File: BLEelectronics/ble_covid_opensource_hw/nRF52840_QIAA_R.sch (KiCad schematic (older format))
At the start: 37 parts, among them J3 Conn_02x05_Odd_Even, SW1 NO, SW2 SW_MEC_5G, U5 nRF52840, X1 32MHz, X2 32.768KHZ

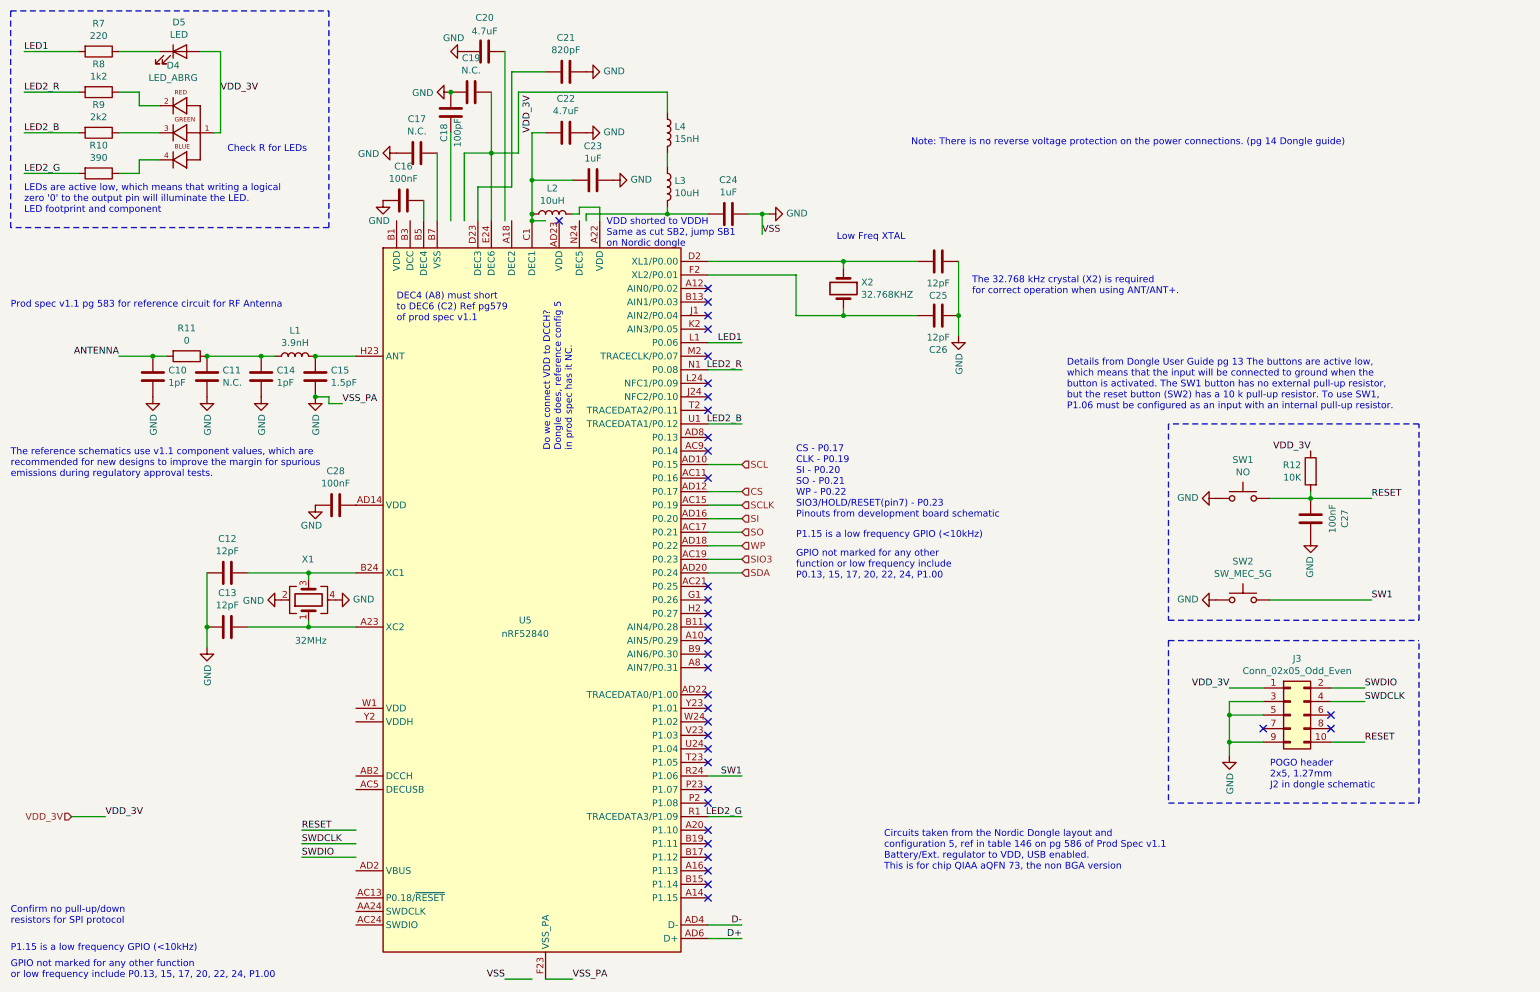
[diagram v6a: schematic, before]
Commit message: schematic updated to be close to the Dongle. Layout update to closer to final footprint. Some traces todo.
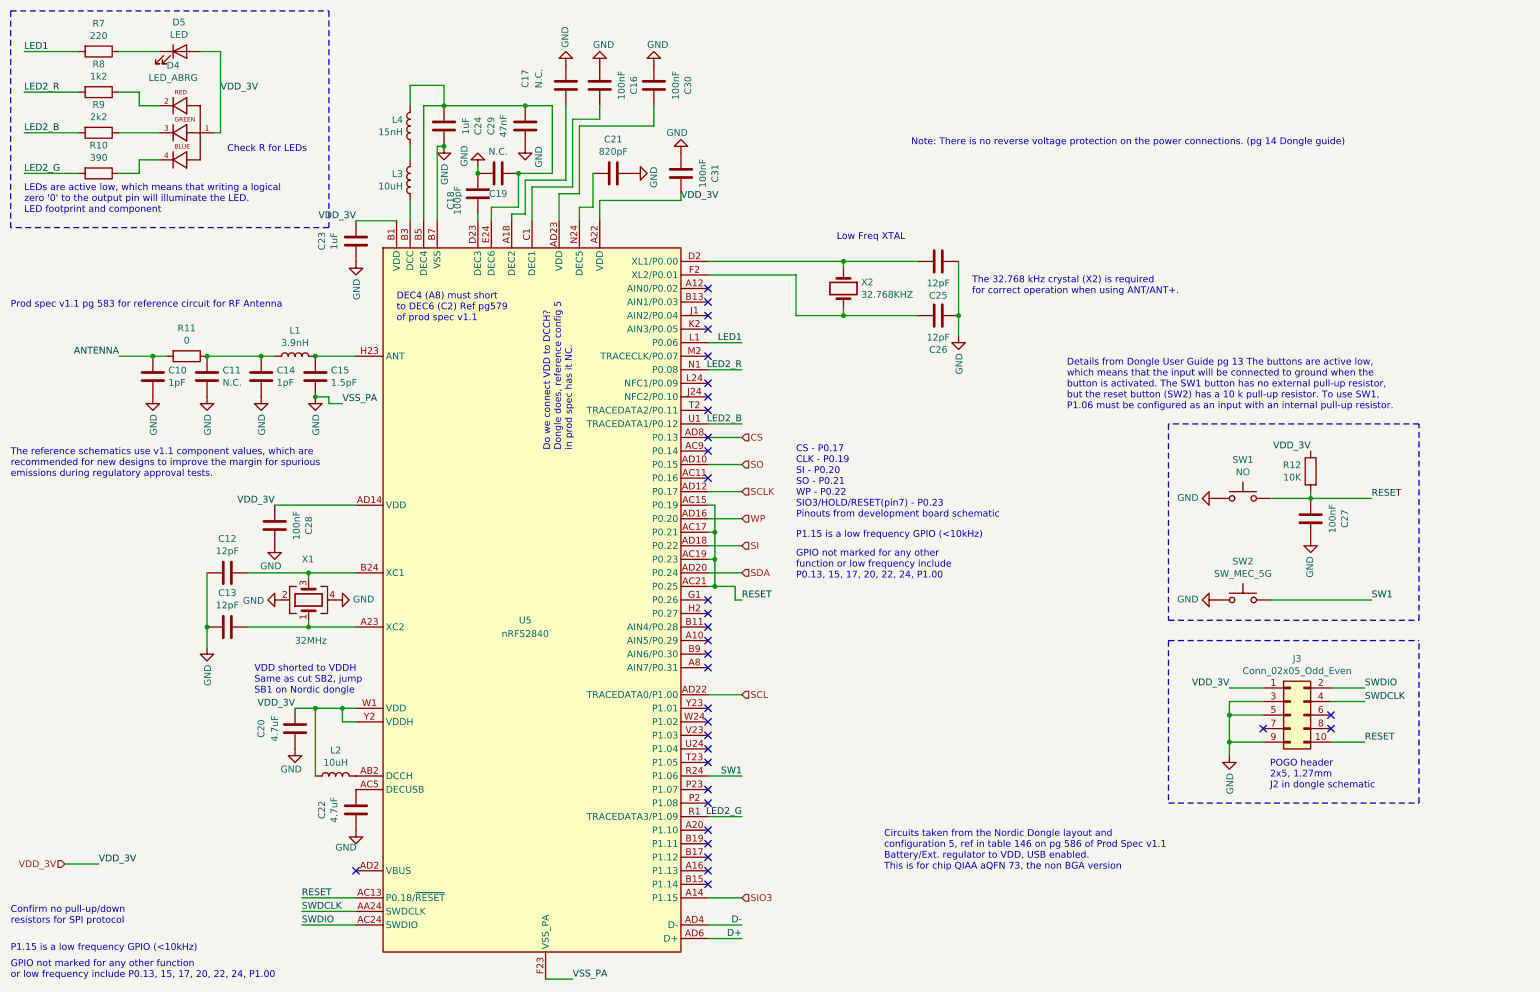
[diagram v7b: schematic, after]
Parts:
- added C29: 47nF, Capacitor_SMD:C_0201_0603Metric, symbol Device:C
- added C30, C31: 100nF, Capacitor_SMD:C_0201_0603Metric, symbol Device:C
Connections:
- net labels removed: VSS
- wire segments 110 -> 132
- no-connect marks 36 -> 33
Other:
- note added: "VDD shorted to VDDH\nSame as cut SB2, jump \nSB1 on Nordic dongle"
- note removed: "VDD shorted to VDDH\nSame as cut SB2, jump SB1\non Nordic dongle"
- moved on the sheet: C16, C17, C18, C19, C20, C21, C22, C23, C24, L2, L3, L4

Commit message: Moved power from pin 3 VBat to pin 8 Vdd on RTC. Swapped SIO3 and SDA on 1a and 1b. Changed battery footprint to allow backside routing for Flash and USB data. Todo: Unbreak MVP1B layout rerouting.
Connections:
- net CS: now also U5.AD10 (P0.15); no longer U5.AD8 (P0.13)
- net SCLK: now also U5.AD16 (P0.20); no longer U5.AD12 (P0.17)
- net SDA: now also U5.A14 (P1.15); no longer U5.AD20 (P0.24)
- net SI: now also U5.AD20 (P0.24); no longer U5.AD18 (P0.22)
- net SIO3: now also U5.AD8 (P0.13); no longer U5.A14 (P1.15)
- net SO: now also U5.AD12 (P0.17); no longer U5.AD10 (P0.15)
- net WP: now also U5.AD18 (P0.22); no longer U5.AD16 (P0.20)
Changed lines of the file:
@@
 	0    -1   -1   0
 $EndComp
-Text Label 6000 7300 2    50   ~ 0
-D-
-Text Label 6000 7400 2    50   ~ 0
-D+
 $Comp
 L power:GND #PWR021
@@
 Text HLabel 6000 5600 2    50   Input ~ 0
 SCL
+Text HLabel 6000 3900 2    50   Input ~ 0
+CS
+Text HLabel 6000 4300 2    50   Input ~ 0
+SCLK
+Text HLabel 6000 4700 2    50   Input ~ 0
+SI
+Text HLabel 6000 4100 2    50   Input ~ 0
+SO
+Text HLabel 6000 4500 2    50   Input ~ 0
+WP
 Text HLabel 6000 3700 2    50   Input ~ 0
-CS
-Text HLabel 6000 4100 2    50   Input ~ 0
-SCLK
-Text HLabel 6000 4500 2    50   Input ~ 0
-SI
-Text HLabel 6000 3900 2    50   Input ~ 0
-SO
-Text HLabel 6000 4300 2    50   Input ~ 0
-WP
+SIO3
 Text HLabel 6000 7100 2    50   Input ~ 0
-SIO3
-Text HLabel 6000 4700 2    50   Input ~ 0
 SDA
 Text Label 1250 6850 0    50   ~ 0
@@
 	5950 4900 6000 4900
 Connection ~ 5800 4800
+Text HLabel 6000 7400 2    50   Input ~ 0
+D+
+Text HLabel 6000 7300 2    50   Input ~ 0
+D-
 $EndSCHEMATC
